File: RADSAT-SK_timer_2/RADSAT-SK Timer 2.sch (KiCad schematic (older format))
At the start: 70 parts, among them J201 Conn_01x07, J202 Conn_01x05_Female, J203 Conn_01x03, J204 Conn_01x02, J205 Conn_01x02, J206 Conn_01x02, J207 Conn_02x26_Odd_Even, J208 Conn_02x26_Odd_Even, Q204 IRLML2060, Q205 IRLML2060, Q206 IRLML2060, SW201 SW_Push, SW202 SW_Push, SW203 SW_Push, SW204 SW_Push, SW205 SW_Push, SW206 SW_Push, U101 LT1521, U102 Galaxia_Timer, U202 TPS3700DDCR, U230 CPC1114N, U240 CPC1114N, U250 CPC1114N, U260 CPC1114N

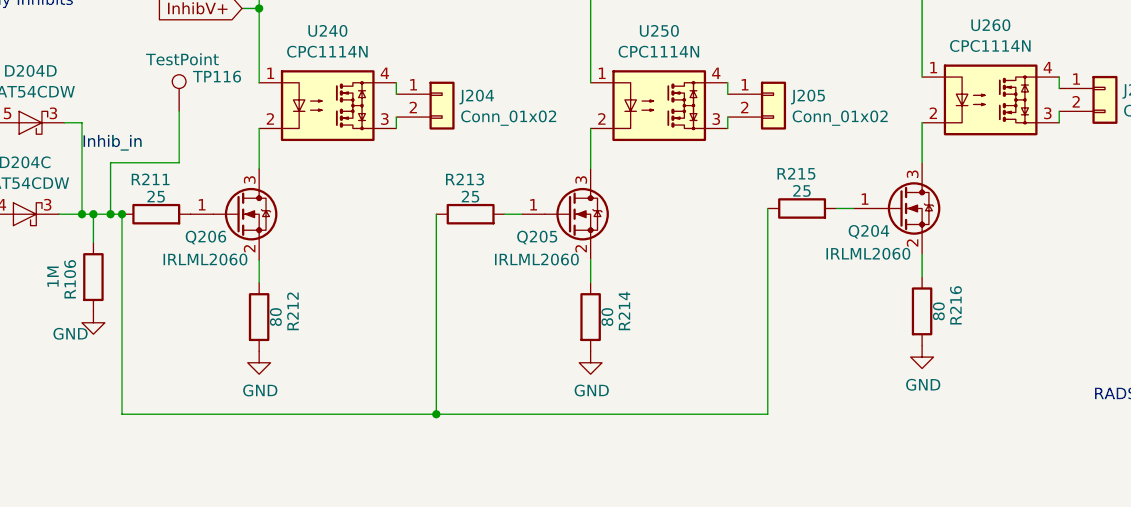
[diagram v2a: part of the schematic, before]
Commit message: places resistor above FET and rerouted PCB
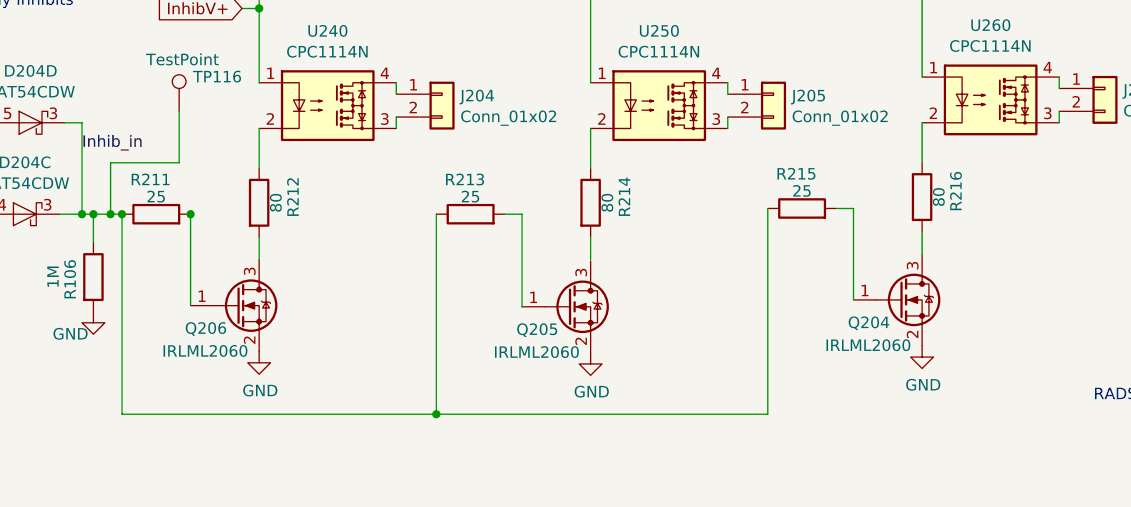
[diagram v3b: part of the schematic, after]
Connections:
- net GND: now also Q204.2 (S), Q205.2 (S), Q206.2 (S); no longer R212.2, R214.2, R216.2
- net at R214.1: now also U250.2; no longer Q205.2 (S)
- net at Q205.3 (D): no longer U250.2
- net at R216.1: now also U260.2; no longer Q204.2 (S)
- net at Q204.3 (D): now also R216.2; no longer U260.2
- net at R212.1: now also U240.2; no longer Q206.2 (S)
- net at Q206.3 (D): now also R212.2; no longer U240.2
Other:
- moved on the sheet: Q204, Q205, Q206, R212, R214, R216
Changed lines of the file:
@@
 L Transistor_FET:IRLML2060 Q204
 U 1 1 6182F8CA
-P 6500 6650
+P 6500 7050
 AR Path="/6182F8CA" Ref="Q204"  Part="1"
 AR Path="/602E25D3/6182F8CA" Ref="Q206"  Part="1"
-F 0 "Q204" H 6275 6550 50  0000 L CNN
-F 1 "IRLML2060" H 6175 6450 50  0000 L CNN
-F 2 "Package_TO_SOT_SMD:SOT-23_Handsoldering" H 6700 6575 50  0001 L CIN
-F 3 "https://www.infineon.com/dgdl/irlml2060pbf.pdf?fileId=5546d462533600a401535664b7fb25ee" H 6500 6650 50  0001 L CNN
-	1    6500 6650
+F 0 "Q204" H 6275 6950 50  0000 L CNN
+F 1 "IRLML2060" H 6175 6850 50  0000 L CNN
+F 2 "Package_TO_SOT_SMD:SOT-23_Handsoldering" H 6700 6975 50  0001 L CIN
+F 3 "https://www.infineon.com/dgdl/irlml2060pbf.pdf?fileId=5546d462533600a401535664b7fb25ee" H 6500 7050 50  0001 L CNN
+	1    6500 7050
 	1    0    0    -1
 $EndComp
@@
 L Device:R R216
 U 1 1 6182F8DF
-P 6600 7100
-F 0 "R216" V 6750 7125 50  0000 C CNN
-F 1 "80" V 6675 7100 50  0000 C CNN
-F 2 "Resistor_SMD:R_0805_2012Metric" V 6530 7100 50  0001 C CNN
-F 3 "~" H 6600 7100 50  0001 C CNN
-	1    6600 7100
+P 6600 6600
+F 0 "R216" V 6750 6625 50  0000 C CNN
+F 1 "80" V 6675 6600 50  0000 C CNN
+F 2 "Resistor_SMD:R_0805_2012Metric" V 6530 6600 50  0001 C CNN
+F 3 "~" H 6600 6600 50  0001 C CNN
+	1    6600 6600
 	1    0    0    -1
 $EndComp
@@
 $EndComp
 Wire Wire Line
-	6600 6850 6600 6950
+	6600 6750 6600 6850
 Wire Wire Line
 	6600 6450 6600 6275
@@
 L Device:R R212
 U 1 1 6183DF42
-P 3700 7125
-F 0 "R212" V 3850 7150 50  0000 C CNN
-F 1 "80" V 3775 7125 50  0000 C CNN
-F 2 "Resistor_SMD:R_0805_2012Metric" V 3630 7125 50  0001 C CNN
-F 3 "~" H 3700 7125 50  0001 C CNN
-	1    3700 7125
-	1    0    0    -1
-$EndComp
-Wire Wire Line
-	3700 6875 3700 6975
+P 3700 6625
+F 0 "R212" V 3850 6650 50  0000 C CNN
+F 1 "80" V 3775 6625 50  0000 C CNN
+F 2 "Resistor_SMD:R_0805_2012Metric" V 3630 6625 50  0001 C CNN
+F 3 "~" H 3700 6625 50  0001 C CNN
+	1    3700 6625
+	1    0    0    -1
+$EndComp
+Wire Wire Line
+	3700 6775 3700 6875
 Wire Wire Line
 	3700 6475 3700 6300
@@
 	1    0    0    -1
 $EndComp
-$Comp
-L Transistor_FET:IRLML2060 Q206
-U 1 1 6183DF2D
-P 3600 6675
-AR Path="/6183DF2D" Ref="Q206"  Part="1"
-AR Path="/602E25D3/6183DF2D" Ref="Q204"  Part="1"
-F 0 "Q206" H 3375 6575 50  0000 L CNN
-F 1 "IRLML2060" H 3275 6475 50  0000 L CNN
-F 2 "Package_TO_SOT_SMD:SOT-23_Handsoldering" H 3800 6600 50  0001 L CIN
-F 3 "https://www.infineon.com/dgdl/irlml2060pbf.pdf?fileId=5546d462533600a401535664b7fb25ee" H 3600 6675 50  0001 L CNN
-	1    3600 6675
-	1    0    0    -1
-$EndComp
-Wire Wire Line
-	5150 6475 5150 6300
-Wire Wire Line
-	5150 6875 5150 6975
+Wire Wire Line
+	5150 6775 5150 6875
 $Comp
 L Relay_SolidState:CPC1117N U250
@@
 	1    0    0    -1
 $EndComp
-$Comp
-L Device:R R214
-U 1 1 6181C5CA
-P 5150 7125
-F 0 "R214" V 5300 7150 50  0000 C CNN
-F 1 "80" V 5225 7125 50  0000 C CNN
-F 2 "Resistor_SMD:R_0805_2012Metric" V 5080 7125 50  0001 C CNN
-F 3 "~" H 5150 7125 50  0001 C CNN
-	1    5150 7125
-	1    0    0    -1
-$EndComp
 Wire Wire Line
 	4775 6675 4850 6675
@@
 L power:GND #PWR0121
 U 1 1 6181C5BF
-P 5150 7275
-F 0 "#PWR0121" H 5150 7025 50  0001 C CNN
-F 1 "GND" H 5155 7102 50  0000 C CNN
-F 2 "" H 5150 7275 50  0001 C CNN
-F 3 "" H 5150 7275 50  0001 C CNN
-	1    5150 7275
+P 5150 7280
+F 0 "#PWR0121" H 5150 7030 50  0001 C CNN
+F 1 "GND" H 5155 7107 50  0000 C CNN
+F 2 "" H 5150 7280 50  0001 C CNN
+F 3 "" H 5150 7280 50  0001 C CNN
+	1    5150 7280
 	1    0    0    -1
 $EndComp
@@
 L Transistor_FET:IRLML2060 Q205
 U 1 1 6181C5B5
-P 5050 6675
+P 5050 7080
 AR Path="/6181C5B5" Ref="Q205"  Part="1"
 AR Path="/602E25D3/6181C5B5" Ref="Q205"  Part="1"
-F 0 "Q205" H 4825 6575 50  0000 L CNN
-F 1 "IRLML2060" H 4725 6475 50  0000 L CNN
-F 2 "Package_TO_SOT_SMD:SOT-23_Handsoldering" H 5250 6600 50  0001 L CIN
-F 3 "https://www.infineon.com/dgdl/irlml2060pbf.pdf?fileId=5546d462533600a401535664b7fb25ee" H 5050 6675 50  0001 L CNN
-	1    5050 6675
+F 0 "Q205" H 4825 6980 50  0000 L CNN
+F 1 "IRLML2060" H 4725 6880 50  0000 L CNN
+F 2 "Package_TO_SOT_SMD:SOT-23_Handsoldering" H 5250 7005 50  0001 L CIN
+F 3 "https://www.infineon.com/dgdl/irlml2060pbf.pdf?fileId=5546d462533600a401535664b7fb25ee" H 5050 7080 50  0001 L CNN
+	1    5050 7080
 	1    0    0    -1
 $EndComp
@@
 Wire Notes Line
 	7950 5425 11220 5425
+$Comp
+L Transistor_FET:IRLML2060 Q206
+U 1 1 6183DF2D
+P 3600 7075
+AR Path="/6183DF2D" Ref="Q206"  Part="1"
+AR Path="/602E25D3/6183DF2D" Ref="Q204"  Part="1"
+F 0 "Q206" H 3375 6975 50  0000 L CNN
+F 1 "IRLML2060" H 3275 6875 50  0000 L CNN
+F 2 "Package_TO_SOT_SMD:SOT-23_Handsoldering" H 3800 7000 50  0001 L CIN
+F 3 "https://www.infineon.com/dgdl/irlml2060pbf.pdf?fileId=5546d462533600a401535664b7fb25ee" H 3600 7075 50  0001 L CNN
+	1    3600 7075
+	1    0    0    -1
+$EndComp
+Wire Wire Line
+	3400 6670 3400 6675
+Connection ~ 3400 6675
+Wire Wire Line
+	3400 6675 3400 7075
+Wire Wire Line
+	5150 6475 5150 6300
+$Comp
+L Device:R R214
+U 1 1 6181C5CA
+P 5150 6625
+F 0 "R214" V 5300 6650 50  0000 C CNN
+F 1 "80" V 5225 6625 50  0000 C CNN
+F 2 "Resistor_SMD:R_0805_2012Metric" V 5080 6625 50  0001 C CNN
+F 3 "~" H 5150 6625 50  0001 C CNN
+	1    5150 6625
+	1    0    0    -1
+$EndComp
+Wire Wire Line
+	4850 6675 4850 7080
+Wire Wire Line
+	6300 6650 6300 7050
 $EndSCHEMATC

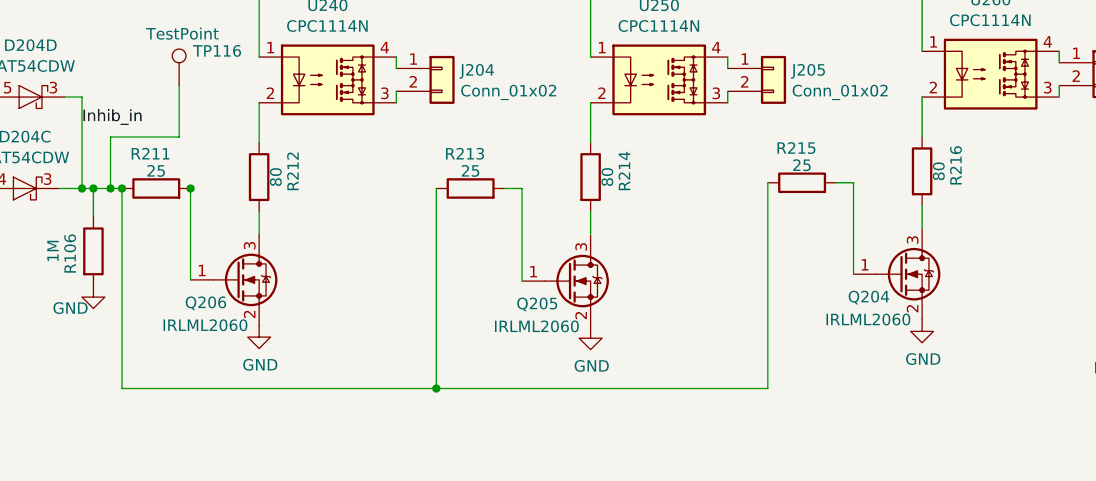
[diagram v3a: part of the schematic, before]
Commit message: fixed relay connection and routed through hole resistor for current divider
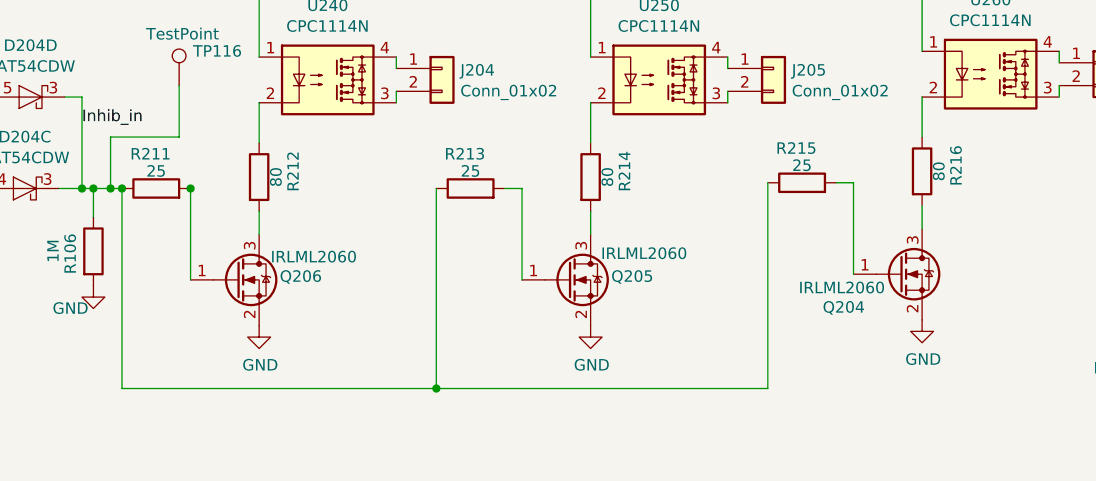
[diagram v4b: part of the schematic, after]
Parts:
- R111: footprint Resistor_SMD:R_0805_2012Metric -> Resistor_THT:R_Axial_DIN0309_L9.0mm_D3.2mm_P12.70mm_Horizontal
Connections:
- net at Q205.3 (D): now also R214.2
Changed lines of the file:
@@
 AR Path="/6182F8CA" Ref="Q204"  Part="1"
 AR Path="/602E25D3/6182F8CA" Ref="Q206"  Part="1"
-F 0 "Q204" H 6275 6950 50  0000 L CNN
-F 1 "IRLML2060" H 6175 6850 50  0000 L CNN
+F 0 "Q204" H 6165 6905 50  0000 L CNN
+F 1 "IRLML2060" H 6060 6990 50  0000 L CNN
 F 2 "Package_TO_SOT_SMD:SOT-23_Handsoldering" H 6700 6975 50  0001 L CIN
 F 3 "https://www.infineon.com/dgdl/irlml2060pbf.pdf?fileId=5546d462533600a401535664b7fb25ee" H 6500 7050 50  0001 L CNN
@@
 L power:GND #PWR0121
 U 1 1 6181C5BF
-P 5150 7280
-F 0 "#PWR0121" H 5150 7030 50  0001 C CNN
-F 1 "GND" H 5155 7107 50  0000 C CNN
-F 2 "" H 5150 7280 50  0001 C CNN
-F 3 "" H 5150 7280 50  0001 C CNN
-	1    5150 7280
+P 5150 7275
+F 0 "#PWR0121" H 5150 7025 50  0001 C CNN
+F 1 "GND" H 5155 7102 50  0000 C CNN
+F 2 "" H 5150 7275 50  0001 C CNN
+F 3 "" H 5150 7275 50  0001 C CNN
+	1    5150 7275
 	1    0    0    -1
 $EndComp
@@
 L Transistor_FET:IRLML2060 Q205
 U 1 1 6181C5B5
-P 5050 7080
+P 5050 7075
 AR Path="/6181C5B5" Ref="Q205"  Part="1"
 AR Path="/602E25D3/6181C5B5" Ref="Q205"  Part="1"
-F 0 "Q205" H 4825 6980 50  0000 L CNN
-F 1 "IRLML2060" H 4725 6880 50  0000 L CNN
-F 2 "Package_TO_SOT_SMD:SOT-23_Handsoldering" H 5250 7005 50  0001 L CIN
-F 3 "https://www.infineon.com/dgdl/irlml2060pbf.pdf?fileId=5546d462533600a401535664b7fb25ee" H 5050 7080 50  0001 L CNN
-	1    5050 7080
+F 0 "Q205" H 5240 7090 50  0000 L CNN
+F 1 "IRLML2060" H 5195 7190 50  0000 L CNN
+F 2 "Package_TO_SOT_SMD:SOT-23_Handsoldering" H 5250 7000 50  0001 L CIN
+F 3 "https://www.infineon.com/dgdl/irlml2060pbf.pdf?fileId=5546d462533600a401535664b7fb25ee" H 5050 7075 50  0001 L CNN
+	1    5050 7075
 	1    0    0    -1
 $EndComp
@@
 F 0 "R111" V 5700 5575 50  0000 R CNN
 F 1 "17" V 5800 5575 50  0000 R CNN
-F 2 "Resistor_SMD:R_0805_2012Metric" V 5830 5525 50  0001 C CNN
+F 2 "Resistor_THT:R_Axial_DIN0309_L9.0mm_D3.2mm_P12.70mm_Horizontal" V 5830 5525 50  0001 C CNN
 F 3 "~" H 5900 5525 50  0001 C CNN
 	1    5900 5525
@@
 AR Path="/6183DF2D" Ref="Q206"  Part="1"
 AR Path="/602E25D3/6183DF2D" Ref="Q204"  Part="1"
-F 0 "Q206" H 3375 6975 50  0000 L CNN
-F 1 "IRLML2060" H 3275 6875 50  0000 L CNN
+F 0 "Q206" H 3790 7090 50  0000 L CNN
+F 1 "IRLML2060" H 3750 7175 50  0000 L CNN
 F 2 "Package_TO_SOT_SMD:SOT-23_Handsoldering" H 3800 7000 50  0001 L CIN
 F 3 "https://www.infineon.com/dgdl/irlml2060pbf.pdf?fileId=5546d462533600a401535664b7fb25ee" H 3600 7075 50  0001 L CNN
@@
 $EndComp
 Wire Wire Line
-	4850 6675 4850 7080
+	4850 6675 4850 7075
 Wire Wire Line
 	6300 6650 6300 7050

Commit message: addded R values
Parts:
- R102: value 604K -> 1.44M
- R103: value 1k -> 2k
- R104: value 2k -> 11k
- R105: value 49.9k -> 81k
- R107: value 81 -> 200
- R108: value 100k -> 160k
- R111: value 17 -> 100
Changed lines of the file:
@@
 AR Path="/62CB5BF2" Ref="R108"  Part="1"
 F 0 "R108" H 6580 5004 50  0000 R CNN
-F 1 "100k" H 6580 5095 50  0000 R CNN
+F 1 "160k" H 6580 5095 50  0000 R CNN
 F 2 "Resistor_SMD:R_0805_2012Metric" V 6580 5050 50  0001 C CNN
 F 3 "~" H 6650 5050 50  0001 C CNN
@@
 AR Path="/62CB5BF8" Ref="R105"  Part="1"
 F 0 "R105" H 6580 4554 50  0000 R CNN
-F 1 "49.9k" H 6580 4645 50  0000 R CNN
+F 1 "81k" H 6580 4645 50  0000 R CNN
 F 2 "Resistor_SMD:R_0805_2012Metric" V 6580 4600 50  0001 C CNN
 F 3 "~" H 6650 4600 50  0001 C CNN
@@
 AR Path="/62CB5BFE" Ref="R102"  Part="1"
 F 0 "R102" H 6580 4079 50  0000 R CNN
-F 1 "604K" H 6580 4170 50  0000 R CNN
+F 1 "1.44M" H 6580 4170 50  0000 R CNN
 F 2 "Resistor_SMD:R_0805_2012Metric" V 6580 4125 50  0001 C CNN
 F 3 "~" H 6650 4125 50  0001 C CNN
@@
 P 975 4950
 F 0 "R103" V 1065 4980 50  0000 L CNN
-F 1 "1k" V 1080 4865 50  0000 L CNN
+F 1 "2k" V 1080 4865 50  0000 L CNN
 F 2 "Resistor_SMD:R_0805_2012Metric" V 905 4950 50  0001 C CNN
 F 3 "~" H 975 4950 50  0001 C CNN
@@
 P 975 5325
 F 0 "R104" H 1045 5371 50  0000 L CNN
-F 1 "2k" H 1045 5280 50  0000 L CNN
+F 1 "11k" H 1045 5280 50  0000 L CNN
 F 2 "Resistor_SMD:R_0805_2012Metric" V 905 5325 50  0001 C CNN
 F 3 "~" H 975 5325 50  0001 C CNN
@@
 AR Path="/62BF960A" Ref="R111"  Part="1"
 F 0 "R111" V 5700 5575 50  0000 R CNN
-F 1 "17" V 5800 5575 50  0000 R CNN
+F 1 "100" V 5800 5575 50  0000 R CNN
 F 2 "Resistor_THT:R_Axial_DIN0309_L9.0mm_D3.2mm_P12.70mm_Horizontal" V 5830 5525 50  0001 C CNN
 F 3 "~" H 5900 5525 50  0001 C CNN
@@
 AR Path="/62C0C9E2" Ref="R107"  Part="1"
 F 0 "R107" H 5850 5025 50  0000 R CNN
-F 1 "81" H 5775 5125 50  0000 R CNN
+F 1 "200" H 5775 5125 50  0000 R CNN
 F 2 "Resistor_SMD:R_0805_2012Metric" V 5530 5075 50  0001 C CNN
 F 3 "~" H 5600 5075 50  0001 C CNN

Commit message: final touches
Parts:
- R110: value 60 -> 40
- R212, R214, R216: value 80 -> 260
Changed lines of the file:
@@
 P 6600 6600
 F 0 "R216" V 6750 6625 50  0000 C CNN
-F 1 "80" V 6675 6600 50  0000 C CNN
+F 1 "260" V 6675 6600 50  0000 C CNN
 F 2 "Resistor_SMD:R_0805_2012Metric" V 6530 6600 50  0001 C CNN
 F 3 "~" H 6600 6600 50  0001 C CNN
@@
 P 3700 6625
 F 0 "R212" V 3850 6650 50  0000 C CNN
-F 1 "80" V 3775 6625 50  0000 C CNN
+F 1 "260" V 3775 6625 50  0000 C CNN
 F 2 "Resistor_SMD:R_0805_2012Metric" V 3630 6625 50  0001 C CNN
 F 3 "~" H 3700 6625 50  0001 C CNN
@@
 P 800 3200
 F 0 "R110" V 593 3200 50  0000 C CNN
-F 1 "60" V 684 3200 50  0000 C CNN
+F 1 "40" V 684 3200 50  0000 C CNN
 F 2 "Resistor_SMD:R_0805_2012Metric" V 730 3200 50  0001 C CNN
 F 3 "~" H 800 3200 50  0001 C CNN
@@
 P 5150 6625
 F 0 "R214" V 5300 6650 50  0000 C CNN
-F 1 "80" V 5225 6625 50  0000 C CNN
+F 1 "260" V 5225 6625 50  0000 C CNN
 F 2 "Resistor_SMD:R_0805_2012Metric" V 5080 6625 50  0001 C CNN
 F 3 "~" H 5150 6625 50  0001 C CNN

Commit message: 555 push for production
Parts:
- removed D102: RB751V40T1G, Diode_SMD:D_SOD-323, symbol Device:D_Schottky
- removed TP111, TP112, TP113, TP114, TP115: TestPoint, S2761-46R:HARWIN_S2761-46R, symbol Connector:TestPoint
- removed U101: LT1521, LT1521IS8-5TR:SO-8_S, symbol LT1521IS8-5TR:LT1521IS8-5TR
- removed U102: Galaxia_Timer, Galaxia_Timer:Galaxia_Timer, symbol Galaxia_Timer:Galaxia_Timer
- removed U202: TPS3700DDCR, Package_TO_SOT_SMD:TSOT-23-6, symbol RADSAT-SK-Timer-rescue:TPS3700DDCR-TPS3700DDCR
- added C104: 600uF, Capacitor_SMD:C_1206_3216Metric, symbol Device:C
- added D101, D102: SBR80520LT1G, Diode_SMD:D_SOD-123, symbol Device:D
- added Q101: 2N7002E, Package_TO_SOT_SMD:SOT-23, symbol Transistor_FET:2N7002E
- added Q102: DSS4240T-7, Package_TO_SOT_SMD:SOT-23, symbol Device:Q_NPN_BCE
- added R112: 0, Resistor_SMD:R_1206_3216Metric_Pad1.30x1.75mm_HandSolder, symbol Device:R
- added R113: 0 or 1k, Resistor_SMD:R_1206_3216Metric_Pad1.30x1.75mm_HandSolder, symbol Device:R
- added U101: TLC555CDR, Package_SO:SOIC-8_3.9x4.9mm_P1.27mm, symbol Timer:TLC555xD
- C101: value 0.1uF -> 10nF; footprint Capacitor_SMD:C_0805_2012Metric -> Capacitor_SMD:C_1206_3216Metric
- C102: value 1uF -> 100uF; footprint Capacitor_SMD:C_0805_2012Metric -> Capacitor_SMD:C_1206_3216Metric
- C103: value 10uF -> 100uF; footprint Capacitor_SMD:C_0805_2012Metric -> Capacitor_SMD:C_1206_3216Metric
- R101: footprint Resistor_SMD:R_0805_2012Metric -> Resistor_SMD:R_1206_3216Metric_Pad1.30x1.75mm_HandSolder
- R102: value 1.44M -> 18M; footprint Resistor_SMD:R_0805_2012Metric -> Resistor_SMD:R_1206_3216Metric_Pad1.30x1.75mm_HandSolder
- R103: value 2k -> 1M; footprint Resistor_SMD:R_0805_2012Metric -> Resistor_SMD:R_1206_3216Metric_Pad1.30x1.75mm_HandSolder
- R104: value 11k -> 0; footprint Resistor_SMD:R_0805_2012Metric -> Resistor_SMD:R_1206_3216Metric_Pad1.30x1.75mm_HandSolder
- R105: value 81k -> 0; footprint Resistor_SMD:R_0805_2012Metric -> Resistor_SMD:R_1206_3216Metric_Pad1.30x1.75mm_HandSolder
- R107: value 200 -> 0; footprint Resistor_SMD:R_0805_2012Metric -> Resistor_SMD:R_1206_3216Metric_Pad1.30x1.75mm_HandSolder
- R108: value 160k -> 3M or 3k6; footprint Resistor_SMD:R_0805_2012Metric -> Resistor_SMD:R_1206_3216Metric_Pad1.30x1.75mm_HandSolder
- R111: value 100 -> 0; footprint Resistor_THT:R_Axial_DIN0309_L9.0mm_D3.2mm_P12.70mm_Horizontal -> Resistor_SMD:R_1206_3216Metric_Pad1.30x1.75mm_HandSolder
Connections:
- net CHRG_ON-OFF is gone; now on net GND: R101.2
- net +5V: now also D101.2 (A); no longer C101.1, C102.1, R101.1
- net +BATT: now also R104.2, R107.2; no longer R102.2
- net A: no longer R107.1
- net GND: now also R105.2, Q101.2 (S), Q102.3 (E), U101.1 (GND), U101.2 (TR); no longer C103.2, R104.2, R108.1, R111.1
- net I2C_CLK: now also J208.44 (Pin_44), TP108.1; no longer J208.43 (Pin_43), TP110.1
- net I2C_DATA: now also J208.42 (Pin_42), TP110.1; no longer J208.41 (Pin_41), TP108.1
- net Inhib_EN: now also R101.1, R111.2, D101.1 (K), R112.1, R113.1
- net USB_Charge: now also J208.31 (Pin_31); no longer J208.32 (Pin_32)
- net at R103.1: now also Q101.3 (D), R112.2; no longer C103.1
- net at R103.2: now also R102.1, R111.1, D102.1 (K), U101.4 (R), U101.8 (VCC); no longer R104.1
- net at R105.1: now also C103.2, R108.1, C104.2; no longer R108.2
- new net: Q101.1 (G), U101.3 (Q)
- new net: C101.1, U101.5 (CV)
- new net: C102.1, R102.2, U101.6 (THR), U101.7 (DIS)
- new net: D102.2 (A), R104.1
- new net: Q102.1 (B), R108.2
- new net: C103.1, C104.1, Q102.2 (C), R107.1, R113.2
- no-connect marks 115 -> 95
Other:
- note added: "10k Pull up\n"
- note added: "555 Timer"
- note added: "DNP, to be tested"
- note added: "Low voltage drop, more \nthan 5V reverse breakdown\n voltage\n"
- note added: "RC Transistor Delay \n"
- note added: "Reverse breakdown of more \nthan 5V to prevent \n+BATT shorting with 5V line\n"
- note added: "to be tested\n"
- note removed: "Atharva Kulkarni\nRiley Nemetz\n"
- note removed: "Battery Charging\n"
- note removed: "Galaxia Timer\n"
- note removed: "June 12 2022"
- note removed: "RADSAT-SK Timer Schematic 2"
- moved on the sheet: D204C, D204D, H101, H102, H103, H104, J201, J204, J205, J206, Q204, Q205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
